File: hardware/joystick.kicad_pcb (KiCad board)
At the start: 2 copper layers, 45 x 25 mm, 18 parts, among them P1 CON-SENSOR, U1 M24C64, U2 NC7WB66K8X, U3 JOYSTICK_BUTTON, U4 DRILL, U5 DRILL, U6 DRILL, U7 DRILL

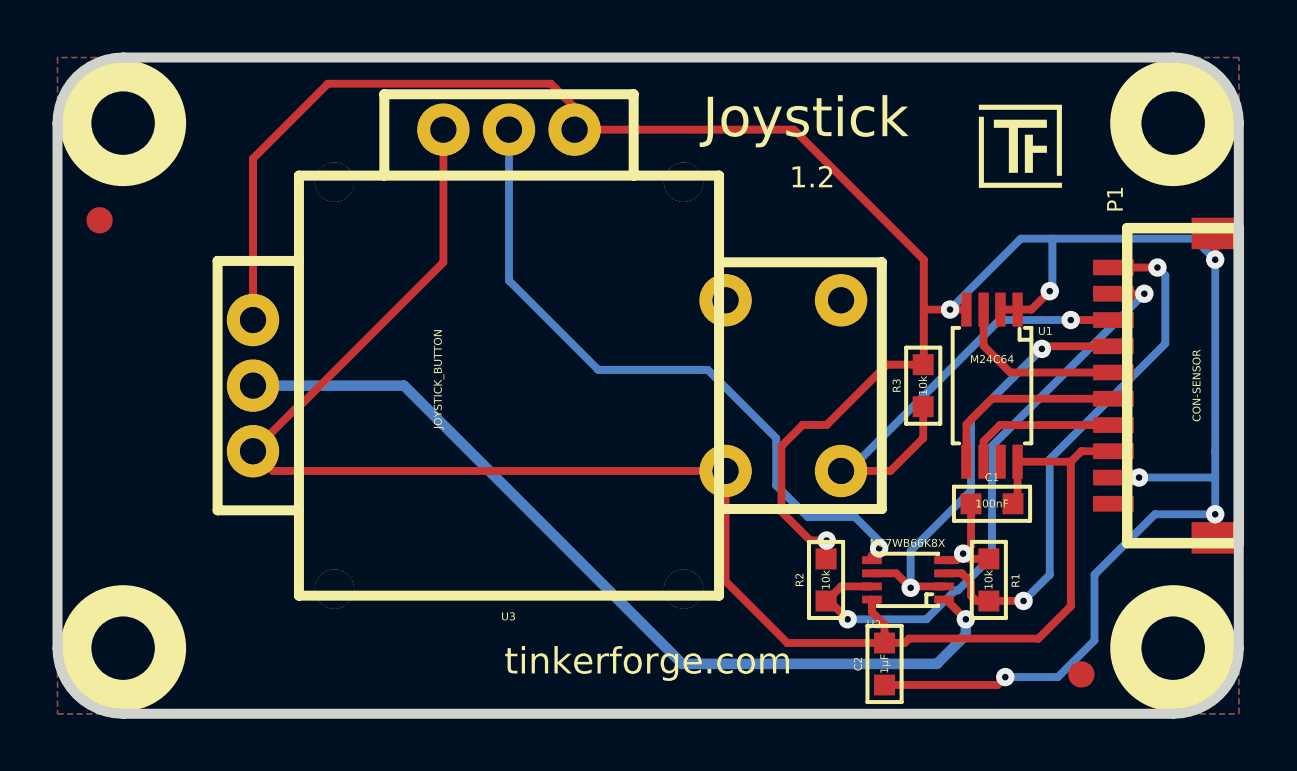
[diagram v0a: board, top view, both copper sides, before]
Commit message: Add 3d information
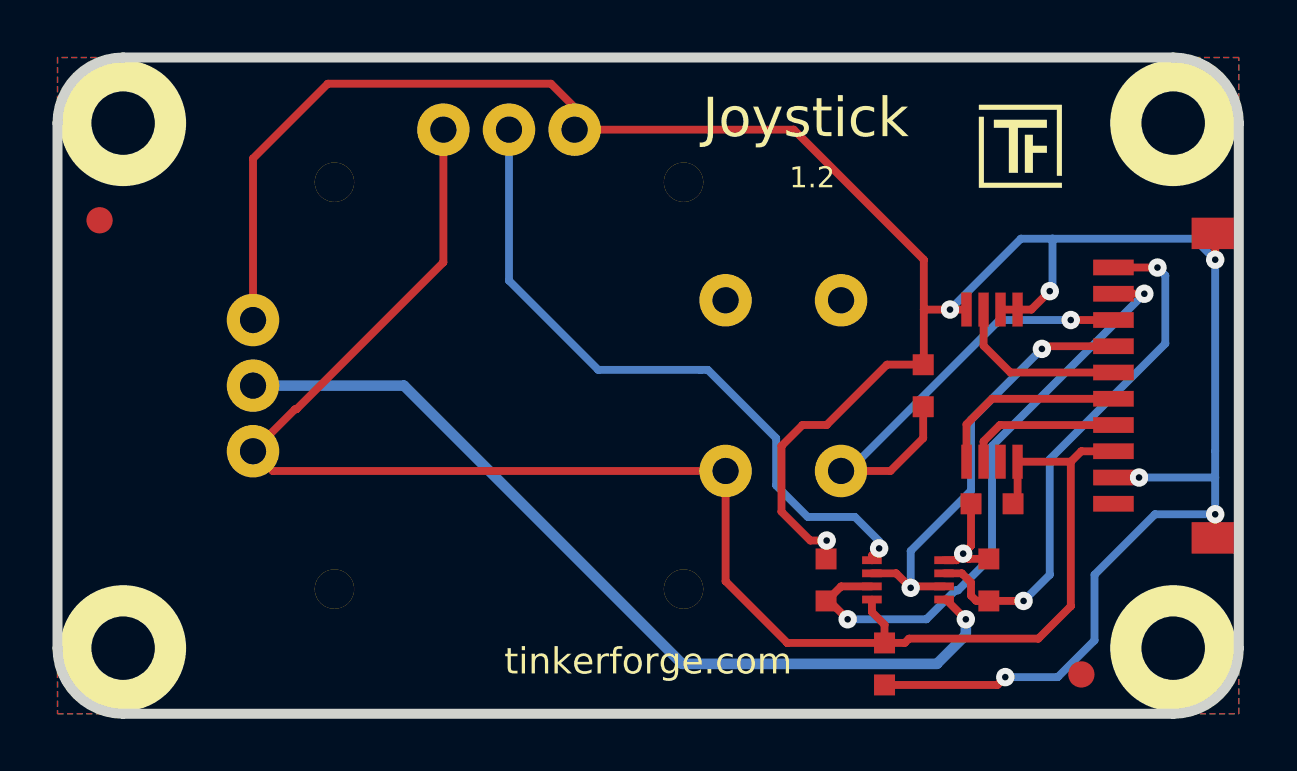
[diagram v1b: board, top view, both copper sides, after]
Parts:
- C1, C2: footprint 0603 -> C0603
- Fiducial_Mark (x2): footprint Fiducial_Mark -> kicad-libraries:Fiducial_Mark
- R1, R2, R3: footprint 0603 -> R0603
- Ref**: footprint Logo_31x31 -> kicad-libraries:Logo_31x31
- U3: footprint Joystick_Button -> kicad-libraries:Joystick_Button
- VAL: footprint CE_5mm -> kicad-libraries:CE_5mm
- VAL: footprint WEEE_7mm -> kicad-libraries:WEEE_7mm
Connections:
- P1 pad 1: (no net) -> Net-(P1-Pad1)
- U1 pad 7: (no net) -> Net-(U1-Pad7)
